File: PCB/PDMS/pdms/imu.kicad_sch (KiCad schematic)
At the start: 4 parts, among them IC17 ASM330LHHTR

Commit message: Added NTC section with 8-to-1 multiplexer
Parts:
- IC17: footprint LGA-14(2.5X3X0.86) -> (none)
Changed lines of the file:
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@@
       (effects (font (size 1.27 1.27)) (justify left))
     )
-    (property "Footprint" "LGA-14(2.5X3X0.86)" (id 2) (at 114.935 43.18 0)
+    (property "Footprint" "" (id 2) (at 114.935 43.18 0)
       (effects (font (size 1.27 1.27)) (justify left) hide)
     )

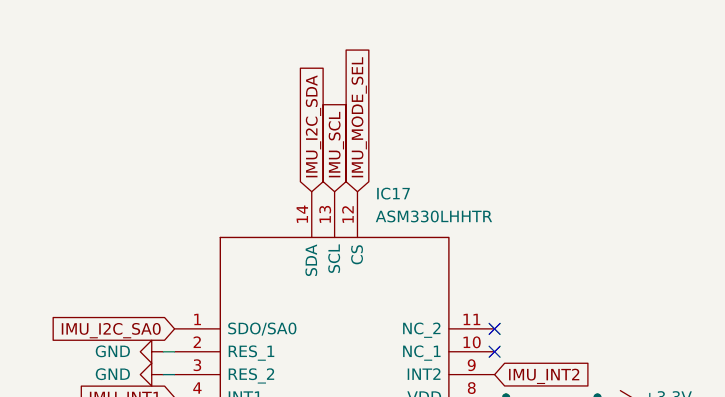
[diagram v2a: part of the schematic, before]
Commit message: Wired IMU on schematics
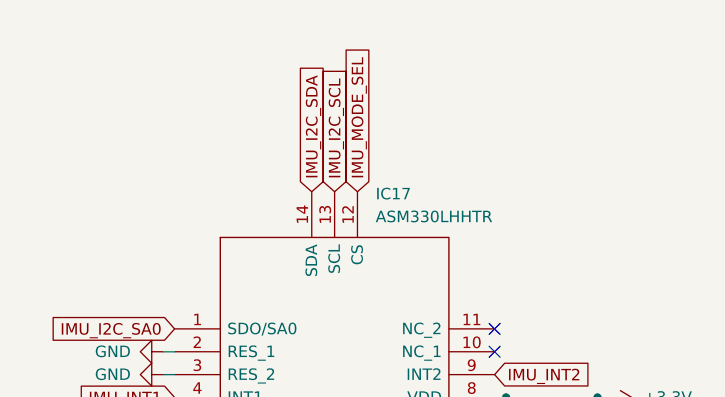
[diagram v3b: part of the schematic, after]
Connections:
- net IMU_SCL renamed IMU_I2C_SCL
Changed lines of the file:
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@@
     )
   )
-  (global_label "IMU_SCL" (shape input) (at 100.965 38.1 90) (fields_autoplaced)
+  (global_label "IMU_I2C_SCL" (shape input) (at 100.965 38.1 90) (fields_autoplaced)
     (effects (font (size 1.27 1.27)) (justify left))
-    (property "Intersheet References" "${INTERSHEET_REFS}" (id 0) (at 100.8856 27.825 90)
+    (property "Intersheet References" "${INTERSHEET_REFS}" (id 0) (at 100.8856 23.7731 90)
       (effects (font (size 1.27 1.27)) (justify left) hide)
     )

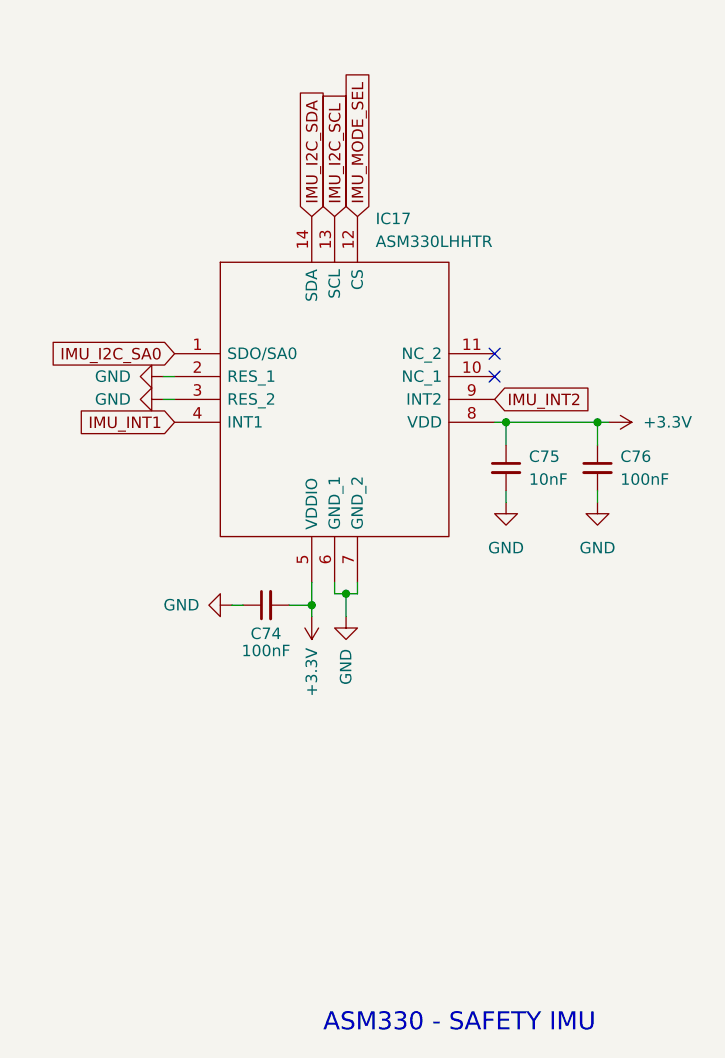
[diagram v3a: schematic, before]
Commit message: Wired all peripherals
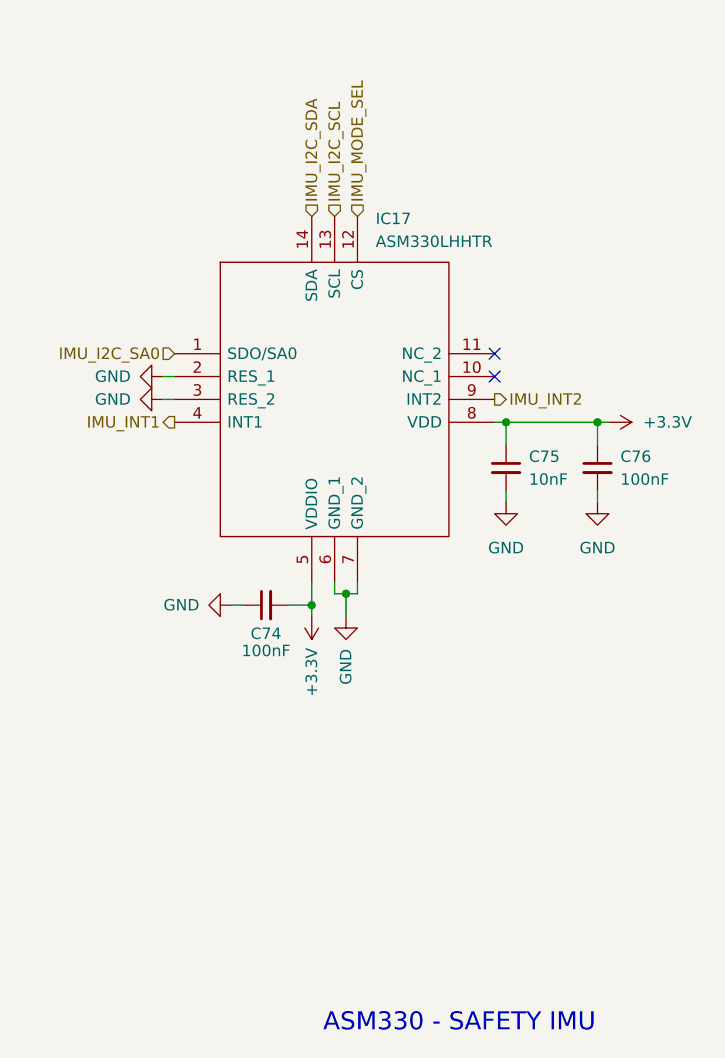
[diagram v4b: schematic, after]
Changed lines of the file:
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@@
     (effects (font (size 2 2)) (justify left bottom))
   )
-  (global_label "IMU_I2C_SA0" (shape input) (at 83.185 53.34 180) (fields_autoplaced)
+  (hierarchical_label "IMU_MODE_SEL" (shape input) (at 103.505 38.1 90)
+    (effects (font (size 1.27 1.27)) (justify left))
+  )
+  (hierarchical_label "IMU_INT2" (shape output) (at 118.745 58.42 0)
+    (effects (font (size 1.27 1.27)) (justify left))
+  )
+  (hierarchical_label "IMU_I2C_SA0" (shape input) (at 83.185 53.34 180)
     (effects (font (size 1.27 1.27)) (justify right))
-    (property "Intersheet References" "${INTERSHEET_REFS}" (id 0) (at 68.8581 53.2606 0)
-      (effects (font (size 1.27 1.27)) (justify right) hide)
-    )
   )
-  (global_label "IMU_I2C_SDA" (shape input) (at 98.425 38.1 90) (fields_autoplaced)
+  (hierarchical_label "IMU_INT1" (shape output) (at 83.185 60.96 180)
+    (effects (font (size 1.27 1.27)) (justify right))
+  )
+  (hierarchical_label "IMU_I2C_SDA" (shape input) (at 98.425 38.1 90)
     (effects (font (size 1.27 1.27)) (justify left))
-    (property "Intersheet References" "${INTERSHEET_REFS}" (id 0) (at 98.3456 23.7126 90)
-      (effects (font (size 1.27 1.27)) (justify left) hide)
-    )
   )
-  (global_label "IMU_I2C_SCL" (shape input) (at 100.965 38.1 90) (fields_autoplaced)
+  (hierarchical_label "IMU_I2C_SCL" (shape input) (at 100.965 38.1 90)
     (effects (font (size 1.27 1.27)) (justify left))
-    (property "Intersheet References" "${INTERSHEET_REFS}" (id 0) (at 100.8856 23.7731 90)
-      (effects (font (size 1.27 1.27)) (justify left) hide)
-    )
-  )
-  (global_label "IMU_MODE_SEL" (shape input) (at 103.505 38.1 90) (fields_autoplaced)
-    (effects (font (size 1.27 1.27)) (justify left))
-    (property "Intersheet References" "${INTERSHEET_REFS}" (id 0) (at 103.4256 21.7774 90)
-      (effects (font (size 1.27 1.27)) (justify left) hide)
-    )
-  )
-  (global_label "IMU_INT2" (shape input) (at 118.745 58.42 0) (fields_autoplaced)
-    (effects (font (size 1.27 1.27)) (justify left))
-    (property "Intersheet References" "${INTERSHEET_REFS}" (id 0) (at 129.6248 58.3406 0)
-      (effects (font (size 1.27 1.27)) (justify left) hide)
-    )
-  )
-  (global_label "IMU_INT1" (shape input) (at 83.185 60.96 180) (fields_autoplaced)
-    (effects (font (size 1.27 1.27)) (justify right))
-    (property "Intersheet References" "${INTERSHEET_REFS}" (id 0) (at 72.3052 60.8806 0)
-      (effects (font (size 1.27 1.27)) (justify right) hide)
-    )
   )
   (symbol (lib_id "power:GND") (at 130.175 69.85 0) (unit 1)

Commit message: Mostly assigned footprints
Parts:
- C74, C75, C76: footprint (none) -> Capacitor_SMD:C_0402_1005Metric_Pad0.74x0.62mm_HandSolder
- IC17: footprint (none) -> PDMS_Additional:LGA-14_2.5X3X0.86_
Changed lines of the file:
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@@
       (effects (font (size 1.27 1.27)) (justify left))
     )
-    (property "Footprint" "" (id 2) (at 130.175 66.04 0)
+    (property "Footprint" "Capacitor_SMD:C_0402_1005Metric_Pad0.74x0.62mm_HandSolder" (id 2) (at 130.175 66.04 0)
       (effects (font (size 1.27 1.27)) hide)
     )
@@
       (effects (font (size 1.27 1.27)) (justify left))
     )
-    (property "Footprint" "" (id 2) (at 120.015 66.04 0)
+    (property "Footprint" "Capacitor_SMD:C_0402_1005Metric_Pad0.74x0.62mm_HandSolder" (id 2) (at 120.015 66.04 0)
       (effects (font (size 1.27 1.27)) hide)
     )
@@
       (effects (font (size 1.27 1.27)) (justify left))
     )
-    (property "Footprint" "" (id 2) (at 114.935 43.18 0)
+    (property "Footprint" "PDMS_Additional:LGA-14_2.5X3X0.86_" (id 2) (at 114.935 43.18 0)
       (effects (font (size 1.27 1.27)) (justify left) hide)
     )
@@
     (property "Reference" "C74" (id 0) (at 93.345 84.455 90))
     (property "Value" "100nF" (id 1) (at 93.345 86.36 90))
-    (property "Footprint" "" (id 2) (at 93.345 81.28 0)
+    (property "Footprint" "Capacitor_SMD:C_0402_1005Metric_Pad0.74x0.62mm_HandSolder" (id 2) (at 93.345 81.28 0)
       (effects (font (size 1.27 1.27)) hide)
     )

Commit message: Flash layout
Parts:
- C74, C75, C76: footprint Capacitor_SMD:C_0402_1005Metric_Pad0.74x0.62mm_HandSolder -> Capacitor_SMD:C_0402_1005Metric
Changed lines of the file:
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@@
       (effects (font (size 1.27 1.27)) (justify left))
     )
-    (property "Footprint" "Capacitor_SMD:C_0402_1005Metric_Pad0.74x0.62mm_HandSolder" (id 2) (at 130.175 66.04 0)
+    (property "Footprint" "Capacitor_SMD:C_0402_1005Metric" (id 2) (at 130.175 66.04 0)
       (effects (font (size 1.27 1.27)) hide)
     )
@@
       (effects (font (size 1.27 1.27)) (justify left))
     )
-    (property "Footprint" "Capacitor_SMD:C_0402_1005Metric_Pad0.74x0.62mm_HandSolder" (id 2) (at 120.015 66.04 0)
+    (property "Footprint" "Capacitor_SMD:C_0402_1005Metric" (id 2) (at 120.015 66.04 0)
       (effects (font (size 1.27 1.27)) hide)
     )
@@
     (property "Reference" "C74" (id 0) (at 93.345 84.455 90))
     (property "Value" "100nF" (id 1) (at 93.345 86.36 90))
-    (property "Footprint" "Capacitor_SMD:C_0402_1005Metric_Pad0.74x0.62mm_HandSolder" (id 2) (at 93.345 81.28 0)
+    (property "Footprint" "Capacitor_SMD:C_0402_1005Metric" (id 2) (at 93.345 81.28 0)
       (effects (font (size 1.27 1.27)) hide)
     )

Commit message: Sub 99 tracks left
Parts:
- added R73, R74: 2k2, Resistor_SMD:R_0402_1005Metric, symbol Device:R_Small
- renumbered IC17 to IC15
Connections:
- net +3.3V: now also R73.1, R74.1
- net IMU_I2C_SCL: now also R74.2
- net IMU_I2C_SDA: now also R73.2
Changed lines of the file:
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@@
   (junction (at 130.175 60.96) (diameter 0) (color 0 0 0 0)
+  )
+  (junction (at 98.425 34.29) (diameter 0) (color 0 0 0 0)
+  )
+  (junction (at 100.965 36.83) (diameter 0) (color 0 0 0 0)
   )
   (junction (at 98.425 81.28) (diameter 0) (color 0 0 0 0)
@@
     (stroke (width 0) (type default) (color 0 0 0 0))
   )
+  (wire (pts (xy 90.17 34.29) (xy 92.075 34.29))
+    (stroke (width 0) (type default) (color 0 0 0 0))
+  )
+  (wire (pts (xy 100.965 32.385) (xy 100.965 36.83))
+    (stroke (width 0) (type default) (color 0 0 0 0))
+  )
   (wire (pts (xy 95.885 81.28) (xy 98.425 81.28))
     (stroke (width 0) (type default) (color 0 0 0 0))
@@
     (stroke (width 0) (type default) (color 0 0 0 0))
   )
+  (wire (pts (xy 98.425 34.29) (xy 98.425 38.1))
+    (stroke (width 0) (type default) (color 0 0 0 0))
+  )
   (wire (pts (xy 130.175 60.96) (xy 130.175 63.5))
     (stroke (width 0) (type default) (color 0 0 0 0))
   )
+  (wire (pts (xy 100.965 36.83) (xy 100.965 38.1))
+    (stroke (width 0) (type default) (color 0 0 0 0))
+  )
+  (wire (pts (xy 97.155 34.29) (xy 98.425 34.29))
+    (stroke (width 0) (type default) (color 0 0 0 0))
+  )
   (wire (pts (xy 89.535 81.28) (xy 90.805 81.28))
     (stroke (width 0) (type default) (color 0 0 0 0))
   )
+  (wire (pts (xy 90.17 36.83) (xy 92.075 36.83))
+    (stroke (width 0) (type default) (color 0 0 0 0))
+  )
   (wire (pts (xy 98.425 81.28) (xy 98.425 78.74))
     (stroke (width 0) (type default) (color 0 0 0 0))
@@
   )
   (wire (pts (xy 102.235 80.01) (xy 102.235 82.55))
+    (stroke (width 0) (type default) (color 0 0 0 0))
+  )
+  (wire (pts (xy 98.425 32.385) (xy 98.425 34.29))
+    (stroke (width 0) (type default) (color 0 0 0 0))
+  )
+  (wire (pts (xy 97.155 36.83) (xy 100.965 36.83))
     (stroke (width 0) (type default) (color 0 0 0 0))
   )
@@
     (effects (font (size 1.27 1.27)) (justify right))
   )
-  (hierarchical_label "IMU_I2C_SDA" (shape input) (at 98.425 38.1 90)
+  (hierarchical_label "IMU_I2C_SDA" (shape input) (at 98.425 32.385 90)
     (effects (font (size 1.27 1.27)) (justify left))
   )
-  (hierarchical_label "IMU_I2C_SCL" (shape input) (at 100.965 38.1 90)
+  (hierarchical_label "IMU_I2C_SCL" (shape input) (at 100.965 32.385 90)
     (effects (font (size 1.27 1.27)) (justify left))
   )
   (symbol (lib_id "power:GND") (at 130.175 69.85 0) (unit 1)
     (in_bom yes) (on_board yes) (fields_autoplaced)
-    (property "Reference" "#PWR0293" (id 0) (at 130.175 76.2 0)
+    (property "Reference" "#PWR0294" (id 0) (at 130.175 76.2 0)
       (effects (font (size 1.27 1.27)) hide)
     )
@@
   (symbol (lib_id "power:+3.3V") (at 98.425 82.55 180) (unit 1)
     (in_bom yes) (on_board yes)
-    (property "Reference" "#PWR0297" (id 0) (at 98.425 78.74 0)
+    (property "Reference" "#PWR0292" (id 0) (at 98.425 78.74 0)
       (effects (font (size 1.27 1.27)) hide)
     )
@@
   (symbol (lib_id "power:GND") (at 120.015 69.85 0) (unit 1)
     (in_bom yes) (on_board yes) (fields_autoplaced)
-    (property "Reference" "#PWR0291" (id 0) (at 120.015 76.2 0)
+    (property "Reference" "#PWR0298" (id 0) (at 120.015 76.2 0)
       (effects (font (size 1.27 1.27)) hide)
     )
@@
     (pin "1")
   )
+  (symbol (lib_id "power:+3.3V") (at 90.17 36.83 90) (unit 1)
+    (in_bom yes) (on_board yes) (fields_autoplaced)
+    (property "Reference" "#PWR0308" (id 0) (at 93.98 36.83 0)
+      (effects (font (size 1.27 1.27)) hide)
+    )
+    (property "Value" "+3.3V" (id 1) (at 86.36 36.8299 90)
+      (effects (font (size 1.27 1.27)) (justify left))
+    )
+    (property "Footprint" "" (id 2) (at 90.17 36.83 0)
+      (effects (font (size 1.27 1.27)) hide)
+    )
+    (property "Datasheet" "" (id 3) (at 90.17 36.83 0)
+      (effects (font (size 1.27 1.27)) hide)
+    )
+    (pin "1")
+  )
+  (symbol (lib_id "Device:R_Small") (at 94.615 34.29 90) (unit 1)
+    (in_bom yes) (on_board yes) (fields_autoplaced)
+    (property "Reference" "R73" (id 0) (at 94.615 27.94 90))
+    (property "Value" "2k2" (id 1) (at 94.615 30.48 90))
+    (property "Footprint" "Resistor_SMD:R_0402_1005Metric" (id 2) (at 94.615 34.29 0)
+      (effects (font (size 1.27 1.27)) hide)
+    )
+    (property "Datasheet" "~" (id 3) (at 94.615 34.29 0)
+      (effects (font (size 1.27 1.27)) hide)
+    )
+    (pin "1")
+    (pin "2")
+  )
   (symbol (lib_id "pdms_additional:ASM330LHHTR") (at 83.185 53.34 0) (unit 1)
     (in_bom yes) (on_board yes) (fields_autoplaced)
-    (property "Reference" "IC17" (id 0) (at 105.5244 38.354 0)
+    (property "Reference" "IC15" (id 0) (at 105.5244 38.354 0)
       (effects (font (size 1.27 1.27)) (justify left))
     )
@@
   (symbol (lib_id "power:GND") (at 81.915 58.42 270) (unit 1)
     (in_bom yes) (on_board yes)
-    (property "Reference" "#PWR0294" (id 0) (at 75.565 58.42 0)
+    (property "Reference" "#PWR0296" (id 0) (at 75.565 58.42 0)
       (effects (font (size 1.27 1.27)) hide)
     )
@@
     )
     (pin "1")
+  )
+  (symbol (lib_id "Device:R_Small") (at 94.615 36.83 90) (unit 1)
+    (in_bom yes) (on_board yes)
+    (property "Reference" "R74" (id 0) (at 94.615 39.37 90))
+    (property "Value" "2k2" (id 1) (at 94.615 41.91 90))
+    (property "Footprint" "Resistor_SMD:R_0402_1005Metric" (id 2) (at 94.615 36.83 0)
+      (effects (font (size 1.27 1.27)) hide)
+    )
+    (property "Datasheet" "~" (id 3) (at 94.615 36.83 0)
+      (effects (font (size 1.27 1.27)) hide)
+    )
+    (pin "1")
+    (pin "2")
   )
   (symbol (lib_id "Device:C_Small") (at 93.345 81.28 90) (unit 1)
@@
     (pin "2")
   )
+  (symbol (lib_id "power:+3.3V") (at 90.17 34.29 90) (unit 1)
+    (in_bom yes) (on_board yes) (fields_autoplaced)
+    (property "Reference" "#PWR0307" (id 0) (at 93.98 34.29 0)
+      (effects (font (size 1.27 1.27)) hide)
+    )
+    (property "Value" "+3.3V" (id 1) (at 86.36 34.2899 90)
+      (effects (font (size 1.27 1.27)) (justify left))
+    )
+    (property "Footprint" "" (id 2) (at 90.17 34.29 0)
+      (effects (font (size 1.27 1.27)) hide)
+    )
+    (property "Datasheet" "" (id 3) (at 90.17 34.29 0)
+      (effects (font (size 1.27 1.27)) hide)
+    )
+    (pin "1")
+  )
   (symbol (lib_id "power:GND") (at 89.535 81.28 270) (unit 1)
     (in_bom yes) (on_board yes)
-    (property "Reference" "#PWR0298" (id 0) (at 83.185 81.28 0)
+    (property "Reference" "#PWR0295" (id 0) (at 83.185 81.28 0)
       (effects (font (size 1.27 1.27)) hide)
     )
@@
   (symbol (lib_id "power:GND") (at 102.235 82.55 0) (unit 1)
     (in_bom yes) (on_board yes)
-    (property "Reference" "#PWR0296" (id 0) (at 102.235 88.9 0)
+    (property "Reference" "#PWR0291" (id 0) (at 102.235 88.9 0)
       (effects (font (size 1.27 1.27)) hide)
     )
@@
   (symbol (lib_id "power:+3.3V") (at 131.445 60.96 270) (unit 1)
     (in_bom yes) (on_board yes) (fields_autoplaced)
-    (property "Reference" "#PWR0292" (id 0) (at 127.635 60.96 0)
+    (property "Reference" "#PWR0293" (id 0) (at 127.635 60.96 0)
       (effects (font (size 1.27 1.27)) hide)
     )
@@
   (symbol (lib_id "power:GND") (at 81.915 55.88 270) (unit 1)
     (in_bom yes) (on_board yes)
-    (property "Reference" "#PWR0295" (id 0) (at 75.565 55.88 0)
-      (effects (font (size 1.27 1.27)) hide)
-    )
+    (property "Reference" "#PWR0297" (id 0) (at 75.565 55.88 0)
+      (effects (font (size 1.27 1.27)) hide)
+    )

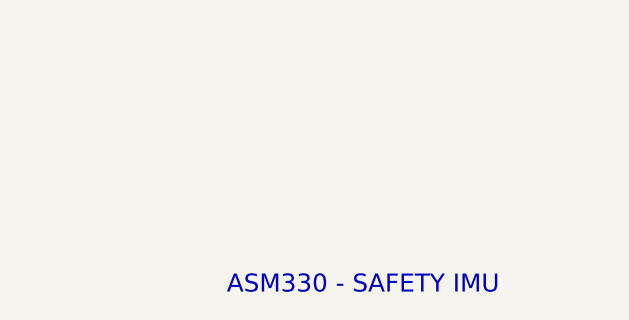
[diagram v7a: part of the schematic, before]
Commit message: WIP PCB folder structure and schematic clean-up
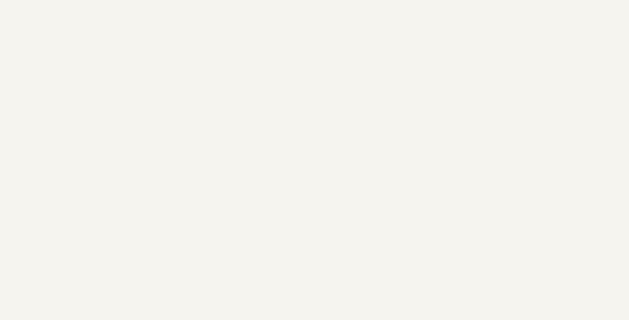
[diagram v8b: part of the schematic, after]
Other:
- note removed: "ASM330 - SAFETY IMU"
- company: (none) -> PGRacing Team
- title: (none) -> ASM330 - SAFETY IMU
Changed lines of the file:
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@@
 (kicad_sch (version 20211123) (generator eeschema)
   (paper "A5")
+  (title_block
+    (title "ASM330 - SAFETY IMU")
+    (rev "V4.2")
+    (company "PGRacing Team")
+    (comment 1 "Karol Pergoł")
+  )
   (junction (at 120.015 60.96) (diameter 0) (color 0 0 0 0)
   )
@@
     (stroke (width 0) (type default) (color 0 0 0 0))
   )
-  (text "ASM330 - SAFETY IMU" (at 99.695 128.905 0)
-    (effects (font (size 2 2)) (justify left bottom))
-  )
   (hierarchical_label "IMU_MODE_SEL" (shape input) (at 103.505 38.1 90)
